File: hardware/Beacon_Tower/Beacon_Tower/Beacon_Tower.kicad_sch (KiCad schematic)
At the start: 2 parts, among them J101 Conn_01x12_Pin, J102 Conn_01x12_Pin

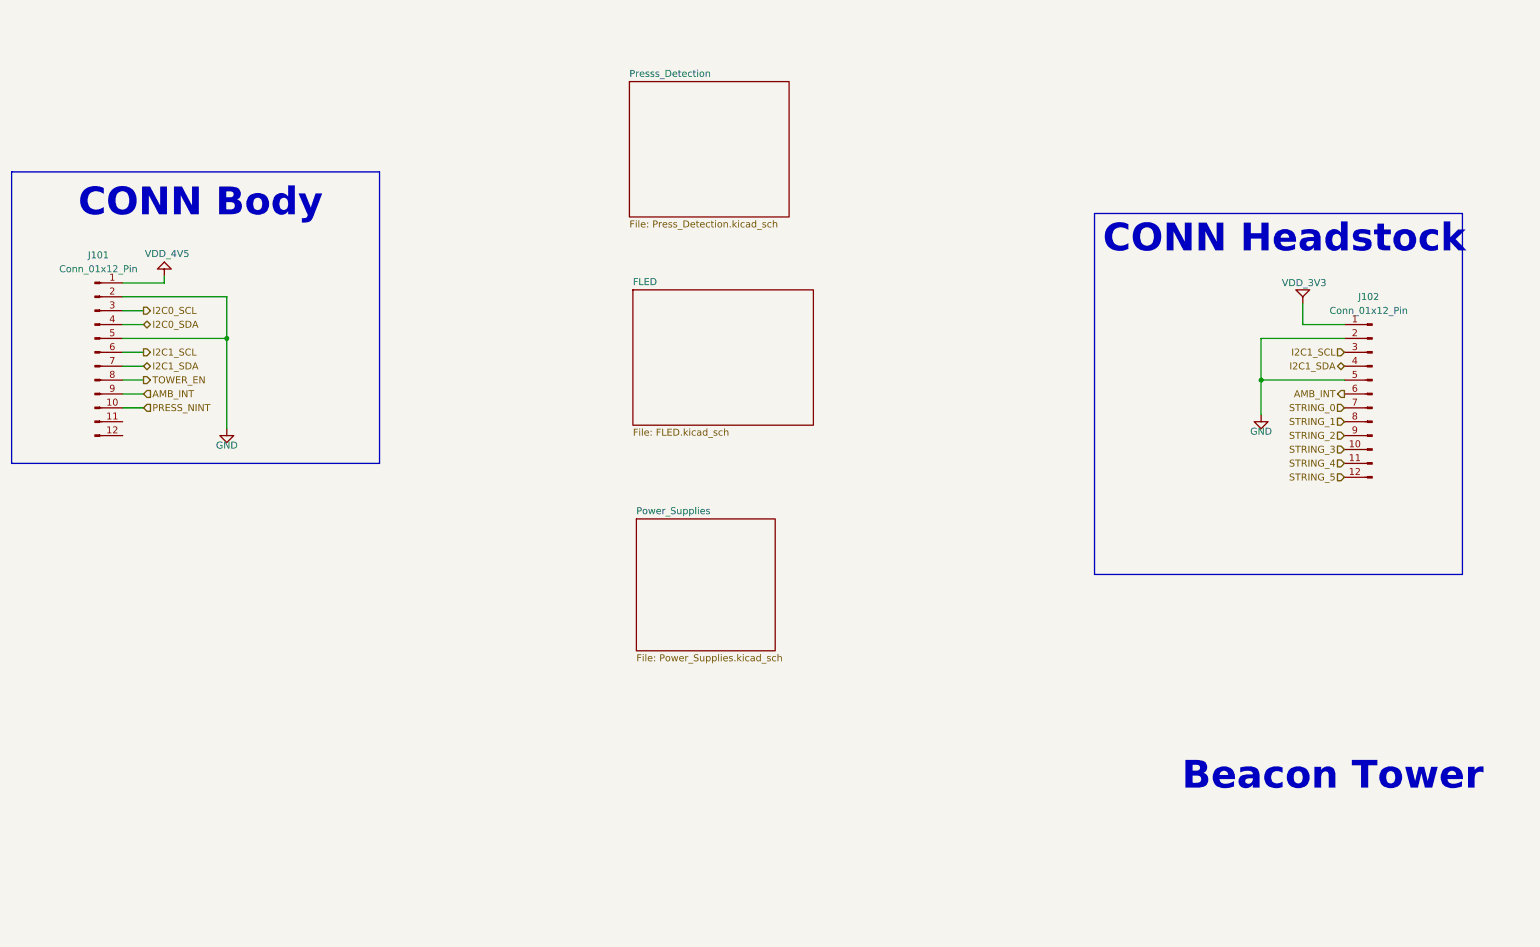
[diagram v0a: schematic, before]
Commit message: Started assigning footprints. Tweaking schematic.
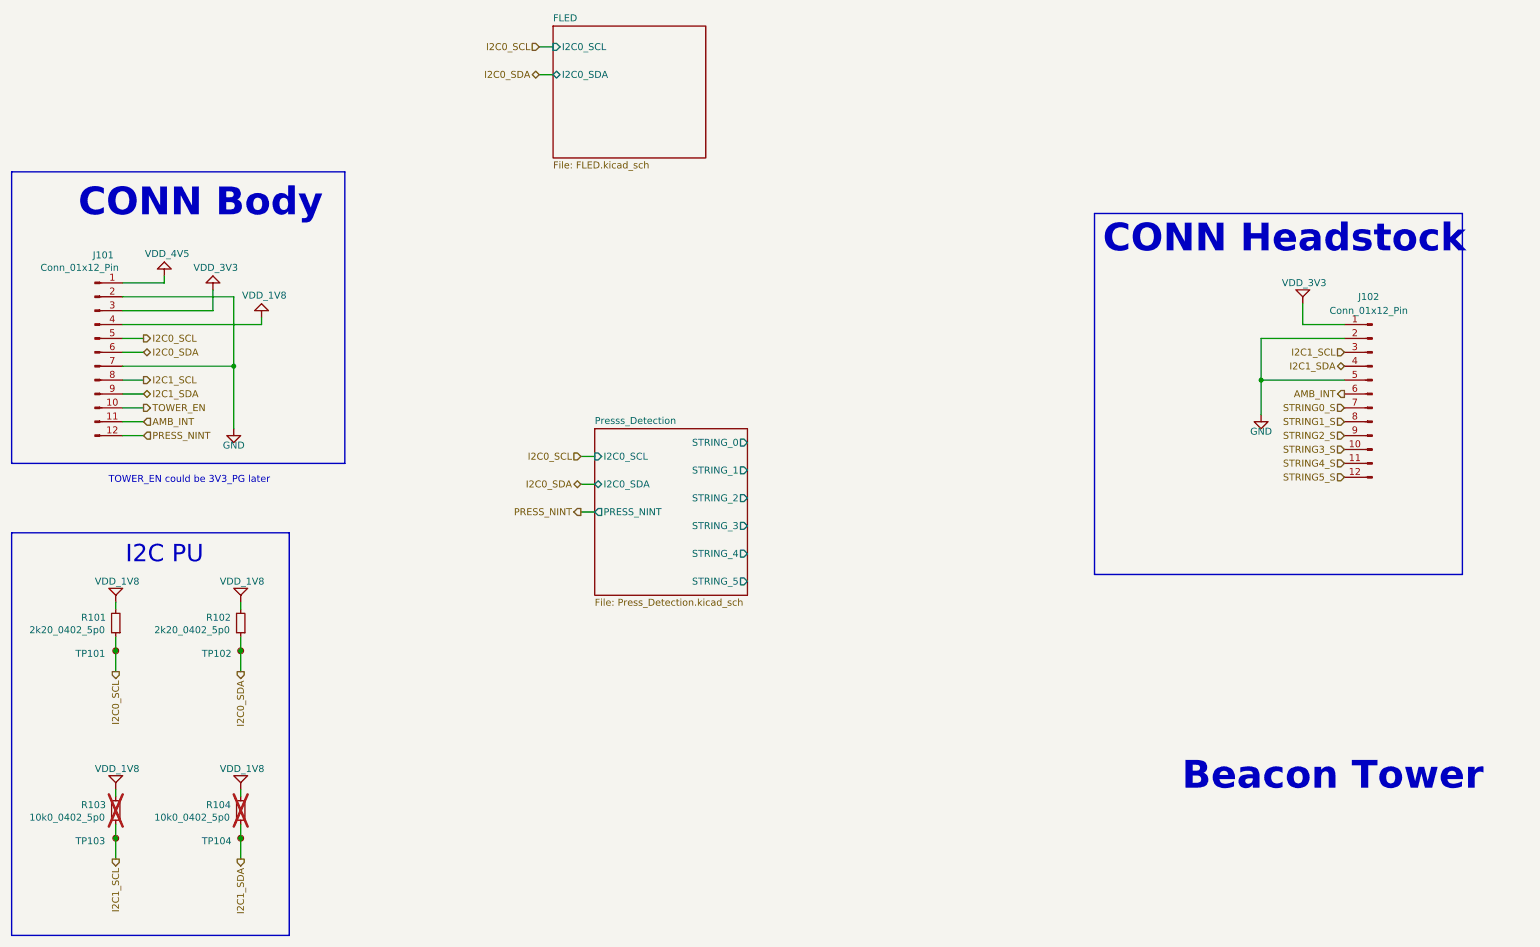
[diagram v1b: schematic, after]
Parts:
- added R101, R102: 2k20_0402_5p0, Resistor_SMD:R_0402_1005Metric, symbol Device:R_Small
- added R103, R104: 10k0_0402_5p0, Resistor_SMD:R_0402_1005Metric, symbol Device:R_Small
- added TP101, TP102, TP103, TP104: TestPoint_Small, TestPoint:TestPoint_Pad_D2.0mm, symbol Connector:TestPoint_Small
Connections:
- net AMB_INT: now also J101.11 (Pin_11); no longer J101.9 (Pin_9)
- net GND: now also J101.7 (Pin_7); no longer J101.5 (Pin_5)
- net I2C0_SCL: now also J101.5 (Pin_5), R101.1, TP101.1; no longer J101.3 (Pin_3)
- net I2C0_SDA: now also J101.6 (Pin_6), R102.1, TP102.1; no longer J101.4 (Pin_4)
- net I2C1_SCL: now also J101.8 (Pin_8), R103.1, TP103.1; no longer J101.6 (Pin_6)
- net I2C1_SDA: now also J101.9 (Pin_9), R104.1, TP104.1; no longer J101.7 (Pin_7)
- net PRESS_NINT: now also J101.12 (Pin_12); no longer J101.10 (Pin_10)
- net TOWER_EN: now also J101.10 (Pin_10); no longer J101.8 (Pin_8)
- net VDD_3V3: now also J101.3 (Pin_3)
- net STRING_0 renamed STRING0_S
- net STRING_1 renamed STRING1_S
- net STRING_2 renamed STRING2_S
- net STRING_3 renamed STRING3_S
- net STRING_4 renamed STRING4_S
- net STRING_5 renamed STRING5_S
- new net VDD_1V8: J101.4 (Pin_4), R101.2, R102.2, R103.2, R104.2
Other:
- removed sheet Power_Supplies
- sheet FLED ports: added I2C0_SCL, I2C0_SDA; removed none
- sheet Presss_Detection ports: added I2C0_SCL, I2C0_SDA, PRESS_NINT, STRING_0, STRING_1, STRING_2, STRING_3, STRING_4, STRING_5; removed none
- note added: "I2C PU"
- note added: "TOWER_EN could be 3V3_PG later"
